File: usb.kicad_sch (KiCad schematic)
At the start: 10 parts, among them J5 USB_A, J8 USB_A, J9 USB_C_Receptacle_USB2.0_16P

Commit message: mostly done except for RTL8305 power stuff
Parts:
- removed R4: 0, Resistor_SMD:R_0402_1005Metric, symbol Device:R
- D8, J5, J8, J9, JP1: now left out of the parts list
- F1, FL1, FL2: now not fitted; now left out of the parts list
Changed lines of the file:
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@@
 	(hierarchical_label "VBUS_DET"
 		(shape output)
-		(at 242.57 71.12 0)
+		(at 234.95 71.12 0)
 		(effects
 			(font
@@
 		(unit 1)
 		(exclude_from_sim no)
-		(in_bom yes)
+		(in_bom no)
 		(on_board yes)
 		(dnp yes)
@@
 		(unit 1)
 		(exclude_from_sim no)
-		(in_bom yes)
-		(on_board yes)
-		(dnp no)
+		(in_bom no)
+		(on_board yes)
+		(dnp yes)
 		(property "Reference" "FL1"
 			(at 228.6 91.44 0)
@@
 		(unit 1)
 		(exclude_from_sim no)
-		(in_bom yes)
-		(on_board yes)
-		(dnp no)
+		(in_bom no)
+		(on_board yes)
+		(dnp yes)
 		(property "Reference" "FL2"
 			(at 110.109 85.09 0)
@@
 		(unit 1)
 		(exclude_from_sim no)
-		(in_bom yes)
+		(in_bom no)
 		(on_board yes)
 		(dnp yes)
@@
 		(unit 1)
 		(exclude_from_sim no)
-		(in_bom yes)
-		(on_board yes)
-		(dnp no)
+		(in_bom no)
+		(on_board yes)
+		(dnp yes)
 		(fields_autoplaced yes)
 		(property "Reference" "F1"
@@
 		(unit 1)
 		(exclude_from_sim no)
-		(in_bom yes)
+		(in_bom no)
 		(on_board yes)
 		(dnp yes)
@@
 	)
 	(symbol
-		(lib_id "Device:R")
-		(at 238.76 71.12 270)
-		(unit 1)
-		(exclude_from_sim no)
-		(in_bom yes)
-		(on_board yes)
-		(dnp no)
-		(property "Reference" "R4"
-			(at 238.76 68.58 90)
-			(effects
-				(font
-					(size 1.27 1.27)
-				)
-			)
-		)
-		(property "Value" "0"
-			(at 238.76 71.12 90)
-			(effects
-				(font
-					(size 1.27 1.27)
-				)
-			)
-		)
-		(property "Footprint" "Resistor_SMD:R_0402_1005Metric"
-			(at 238.76 69.342 90)
-			(effects
-				(font
-					(size 1.27 1.27)
-				)
-				(hide yes)
-			)
-		)
-		(property "Datasheet" "~"
-			(at 238.76 71.12 0)
-			(effects
-				(font
-					(size 1.27 1.27)
-				)
-				(hide yes)
-			)
-		)
-		(property "Description" "Resistor"
-			(at 238.76 71.12 0)
-			(effects
-				(font
-					(size 1.27 1.27)
-				)
-				(hide yes)
-			)
-		)
-		(pin "2"
-		)
-		(pin "1"
-		)
-		(instances
-			(project ""
-				(path "/ebd96e19-6f65-4022-a6da-be26c0716f8e/9ae95502-5895-429a-9658-dcc355299464"
-					(reference "R4")
-					(unit 1)
-				)
-			)
-		)
-	)
-	(symbol
 		(lib_id "power:GND")
 		(at 226.06 78.74 0)
@@
 		(unit 1)
 		(exclude_from_sim no)
-		(in_bom yes)
+		(in_bom no)
 		(on_board yes)
 		(dnp yes)
@@
 		(unit 1)
 		(exclude_from_sim no)
-		(in_bom yes)
+		(in_bom no)
 		(on_board yes)
 		(dnp yes)

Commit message: Finally done the layout
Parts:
- JP1: footprint Connector_PinHeader_1.00mm:PinHeader_1x02_P1.00mm_Vertical -> Connector_PinHeader_2.54mm:PinHeader_1x02_P2.54mm_Vertical
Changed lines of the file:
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@@
 			)
 		)
-		(property "Footprint" "Connector_PinHeader_1.00mm:PinHeader_1x02_P1.00mm_Vertical"
+		(property "Footprint" "Connector_PinHeader_2.54mm:PinHeader_1x02_P2.54mm_Vertical"
 			(at 231.14 115.57 0)
 			(effects

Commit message: finalized board for fabrication
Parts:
- C8: LCSC Part # (none) -> C96446

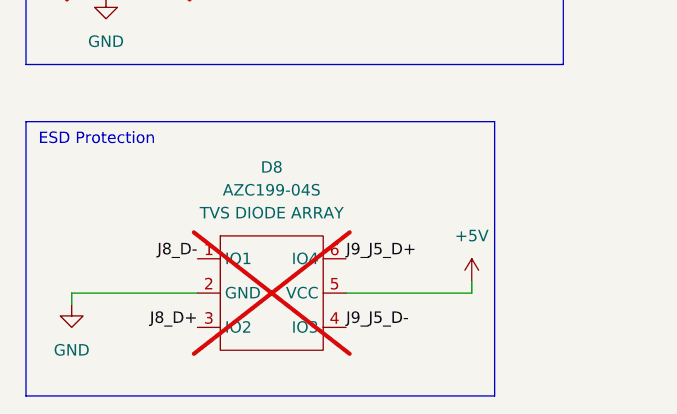
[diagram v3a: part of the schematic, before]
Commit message: fix incorrect footprint orientation and breakout uarts
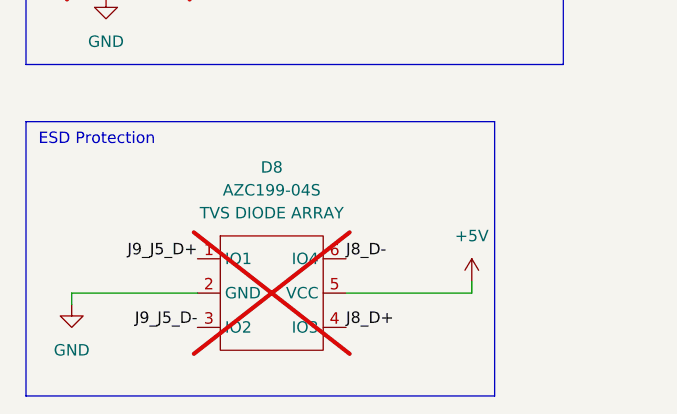
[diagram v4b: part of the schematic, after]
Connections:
- net J8_D+: now also D8.4 (IO3); no longer D8.3 (IO2)
- net J8_D-: now also D8.6 (IO4); no longer D8.1 (IO1)
- net J9_J5_D+: now also D8.1 (IO1); no longer D8.6 (IO4)
- net J9_J5_D-: now also D8.3 (IO2); no longer D8.4 (IO3)
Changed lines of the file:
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@@
 	)
 	(label "J9_J5_D-"
+		(at 90.17 138.43 180)
+		(effects
+			(font
+				(size 1.27 1.27)
+			)
+			(justify right bottom)
+		)
+	)
+	(label "J8_D+"
 		(at 106.68 138.43 0)
 		(effects
@@
 		)
 	)
-	(label "J8_D+"
-		(at 90.17 138.43 180)
+	(label "J8_D-"
+		(at 106.68 130.81 0)
 		(effects
 			(font
 				(size 1.27 1.27)
 			)
-			(justify right bottom)
-		)
-	)
-	(label "J8_D-"
-		(at 90.17 130.81 180)
-		(effects
-			(font
-				(size 1.27 1.27)
-			)
-			(justify right bottom)
+			(justify left bottom)
 		)
 	)
@@
 	)
 	(label "J9_J5_D+"
-		(at 106.68 130.81 0)
+		(at 90.17 130.81 180)
 		(effects
 			(font
 				(size 1.27 1.27)
 			)
-			(justify left bottom)
+			(justify right bottom)
 		)
 	)
